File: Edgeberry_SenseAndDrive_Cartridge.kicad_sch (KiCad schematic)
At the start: 40 parts, among them J1 Screw_Terminal_01x08, J2 Grove, J3 Conn_01x02_Pin, Q1 BC847, Q10 FQD17P06TM, Q11 BC847, Q12 FQD17P06TM, Q13 BS170, Q14 BS170, Q2 FQD17P06TM, Q3 BC847, Q4 FQD17P06TM, Q5 BC847, Q6 FQD17P06TM, Q7 BC847, Q8 FQD17P06TM, Q9 BC847

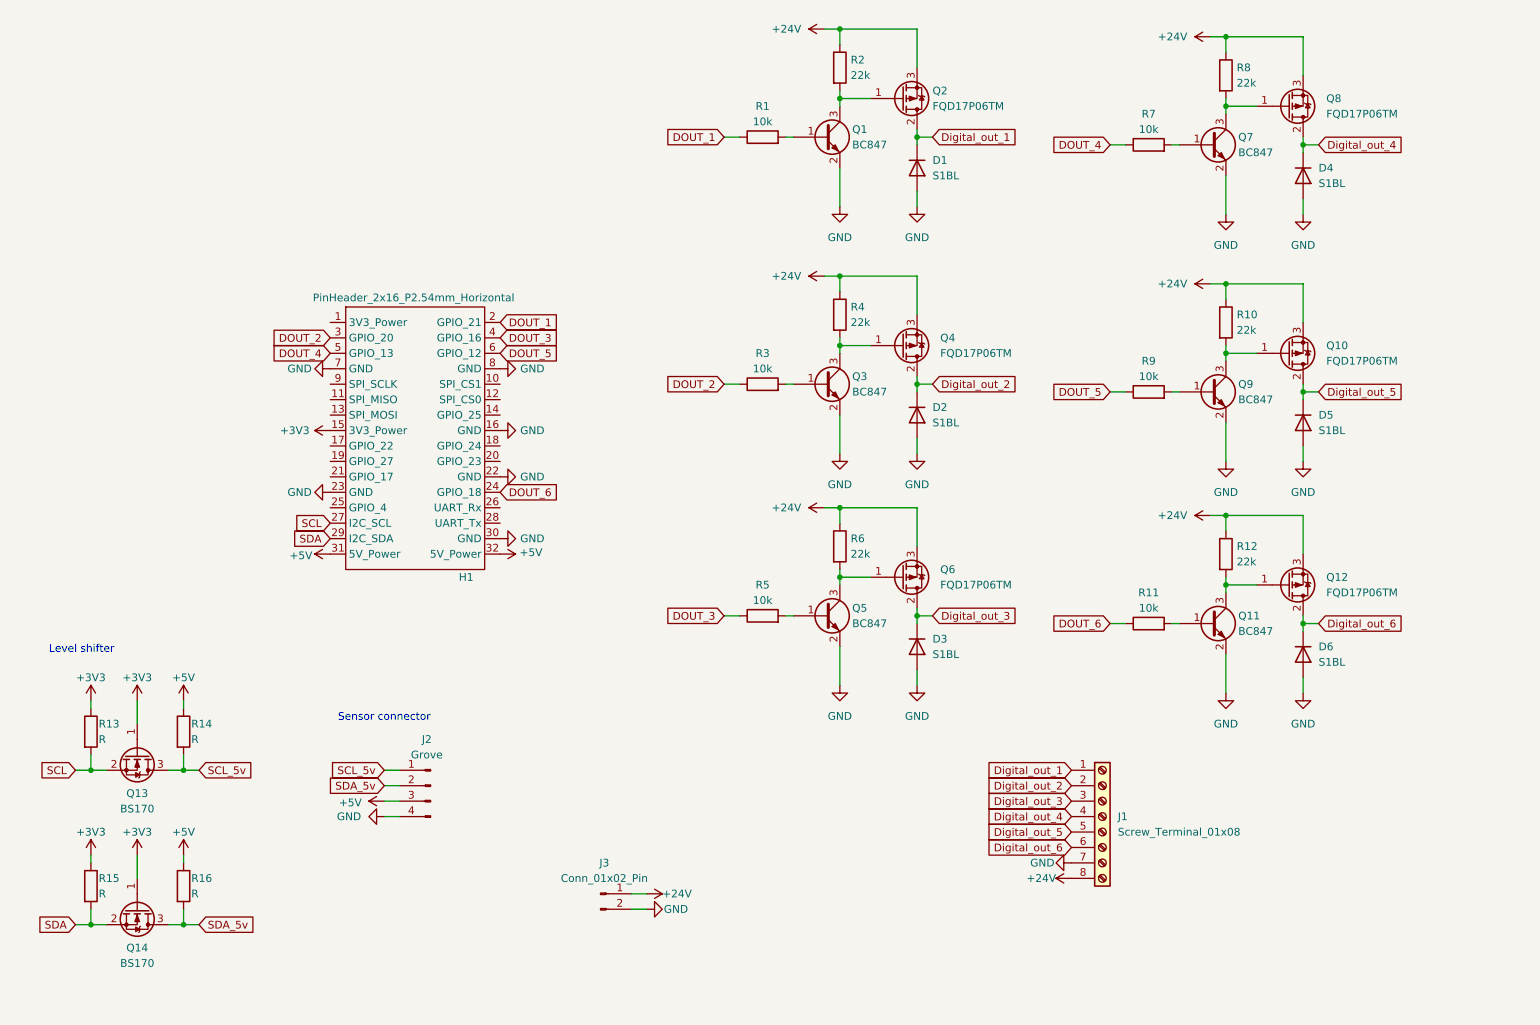
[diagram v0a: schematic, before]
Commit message: Update resistor values
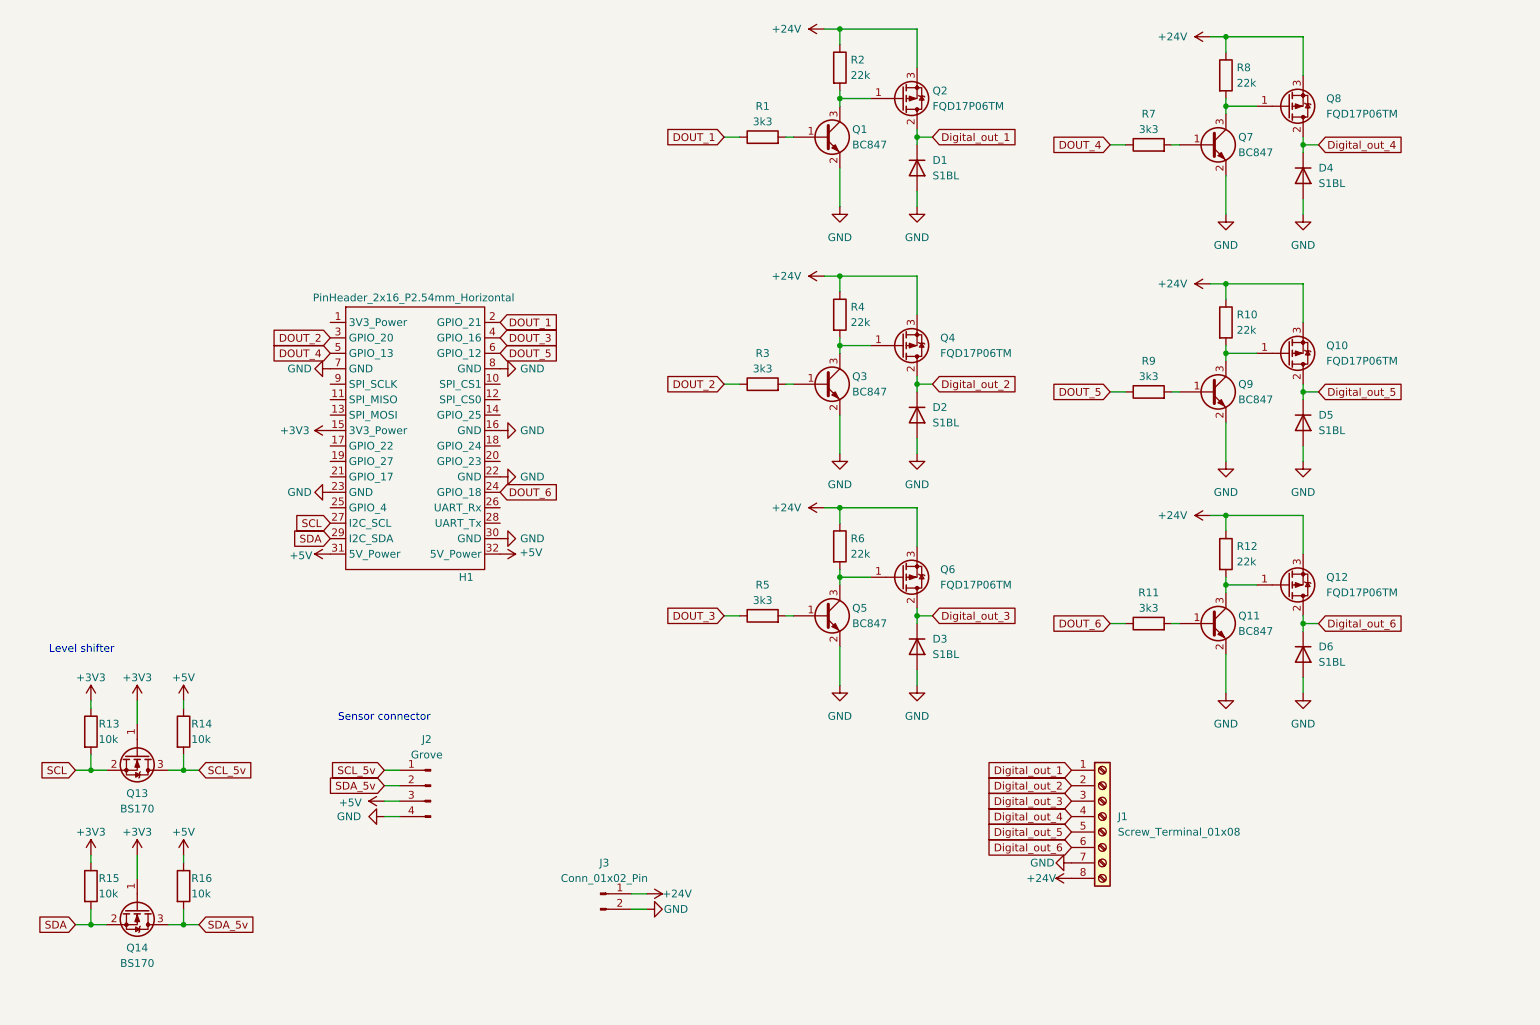
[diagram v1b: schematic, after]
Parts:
- R1, R11, R3, R5, R7, R9: value 10k -> 3k3
- R13, R14, R15, R16: value R -> 10k
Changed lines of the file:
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@@
 			)
 		)
-		(property "Value" "10k"
+		(property "Value" "3k3"
 			(at 158.75 74.93 90)
 			(effects
@@
 			)
 		)
-		(property "Value" "R"
+		(property "Value" "10k"
 			(at 64.77 135.89 0)
 			(effects
@@
 			)
 		)
-		(property "Value" "10k"
+		(property "Value" "3k3"
 			(at 222.25 76.2 90)
 			(effects
@@
 			)
 		)
-		(property "Value" "10k"
+		(property "Value" "3k3"
 			(at 222.25 35.56 90)
 			(effects
@@
 			)
 		)
-		(property "Value" "10k"
+		(property "Value" "3k3"
 			(at 158.75 113.03 90)
 			(effects
@@
 			)
 		)
-		(property "Value" "R"
+		(property "Value" "10k"
 			(at 64.77 161.29 0)
 			(effects
@@
 			)
 		)
-		(property "Value" "10k"
+		(property "Value" "3k3"
 			(at 222.25 114.3 90)
 			(effects
@@
 			)
 		)
-		(property "Value" "R"
+		(property "Value" "10k"
 			(at 49.53 135.89 0)
 			(effects
@@
 			)
 		)
-		(property "Value" "10k"
+		(property "Value" "3k3"
 			(at 158.75 34.29 90)
 			(effects
@@
 			)
 		)
-		(property "Value" "R"
+		(property "Value" "10k"
 			(at 49.53 161.29 0)
 			(effects

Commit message: Version 1.0 cleanup
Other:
- note added: "Copyright© 2024 Sanne 'SpuQ' Santens. This design is released under the CERN OHL-W license on GitHub."
- note added: "EDGEBERRY HARDWARE CARTRIDGE"
- note added: "Edgeberry Hardware Cartridge connector"
- note added: "I2C Sensor port"
- note added: "Sense'n'Drive Cartridge, Rev.: 1.0, mid 2024"
- note added: "Sourcing MOSFET digital outputs"
- moved on the sheet: D1, D2, D3, D4, D5, D6, H1, J1, J2, J3, Q1, Q10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
